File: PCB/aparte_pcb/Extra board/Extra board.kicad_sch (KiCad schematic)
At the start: 4 parts, among them J1 Conn_01x10_Pin, J2 Conn_01x04_Pin, J3 Conn_01x10_Socket, U1 MCP23008-xP

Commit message: extra PCB changes
Multi-line description of commit,
feel free to be detailed.

Signed-off-by: Abel Tim <git@abeltim.com>
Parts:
- removed J3: Conn_01x10_Socket, symbol Connector:Conn_01x10_Socket
- added J3: Conn_01x10_Pin, symbol Connector:Conn_01x10_Pin
- added J4: Conn_01x04_Pin, symbol Connector:Conn_01x04_Pin
- added U2: MCP23017_SP, Package_DIP:DIP-28_W7.62mm, symbol Interface_Expansion:MCP23017_SP
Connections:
- net 5v: now also J2.3 (Pin_3), U1.9 (VSS), J4.3 (Pin_3), U2.10 (VSS); no longer J2.1 (Pin_1), U1.18 (VDD)
- net GND: now also U1.18 (VDD), U1.3 (A2), U1.4 (A1), U1.5 (A0), J4.2 (Pin_2), U2.15 (A0), U2.16 (A1), U2.17 (A2), U2.9 (VDD); no longer U1.9 (VSS)
- net Groen: now also J3.1 (Pin_1); no longer J1.1 (Pin_1), U1.2 (SDA)
- net Rood: now also J3.2 (Pin_2); no longer J1.2 (Pin_2), U1.1 (SCL)
- net blauw: now also J4.1 (Pin_1); no longer J2.3 (Pin_3)
- net pr1: now also J3.10 (Pin_10); no longer J1.10 (Pin_10)
- net pr2: now also J3.9 (Pin_9); no longer J1.9 (Pin_9)
- net pr3: now also J3.8 (Pin_8); no longer J1.8 (Pin_8)
- net pr4: now also J3.7 (Pin_7); no longer J1.7 (Pin_7)
- net pr5: now also J3.6 (Pin_6); no longer J1.6 (Pin_6)
- net pr6: now also J3.5 (Pin_5); no longer J1.5 (Pin_5)
- net pr7: now also J3.4 (Pin_4); no longer J1.4 (Pin_4)
- net pr8: now also J3.3 (Pin_3); no longer J1.3 (Pin_3)
- new net SCL: J1.1 (Pin_1), U1.1 (SCL), U2.12 (SCK)
- new net SDA: J2.1 (Pin_1), U1.2 (SDA), U2.13 (SDA)
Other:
- note added: "LOWER BOARD CONNECTOR"
- note added: "MIDDLE BOARD CONNECTOR"
- moved on the sheet: J2

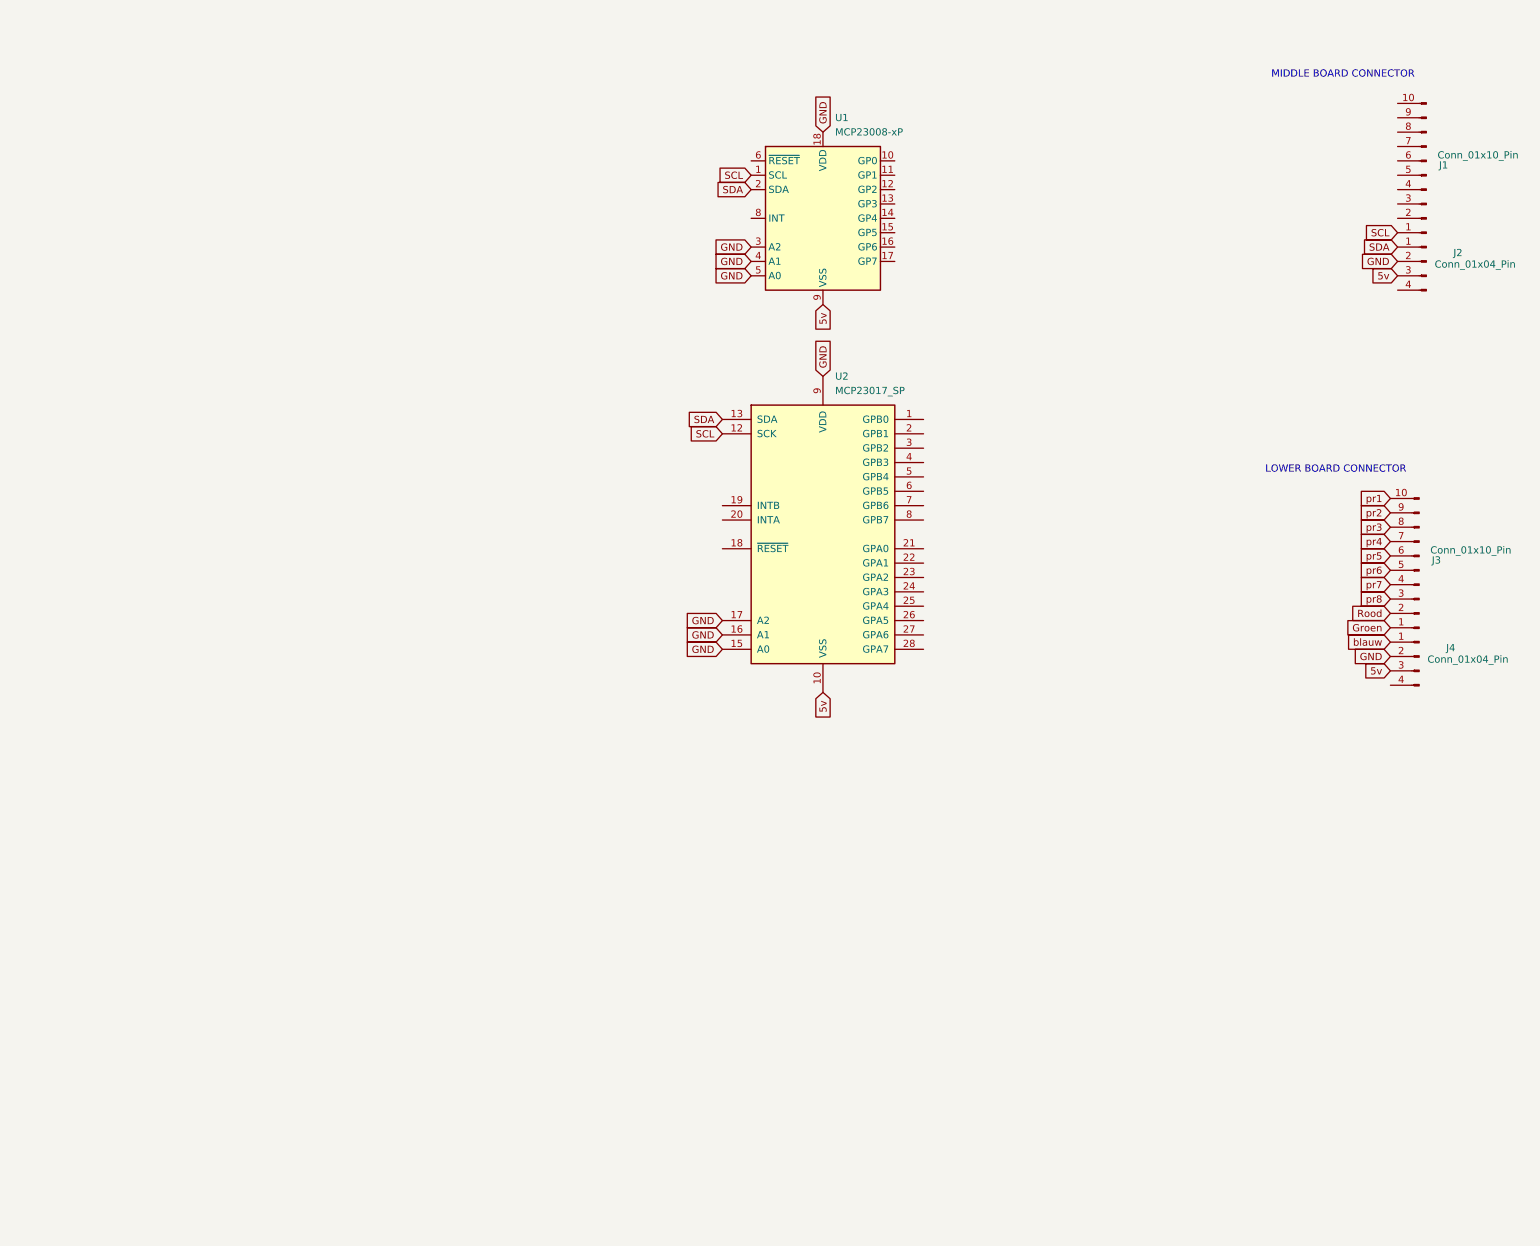
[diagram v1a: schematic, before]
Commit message: almost finished extra pcb
The pcb is designed to be single layerd for simplisity, but there are still two unconnected lines, GND and 5V are now both in two seperate sections. Can connect via an wire or update the PCB. Will not spend a lot of time on it now for it is not shure we will use an PCB or just a board with lots of wires on it.

Signed-off-by: Abel Tim <git@abeltim.com>
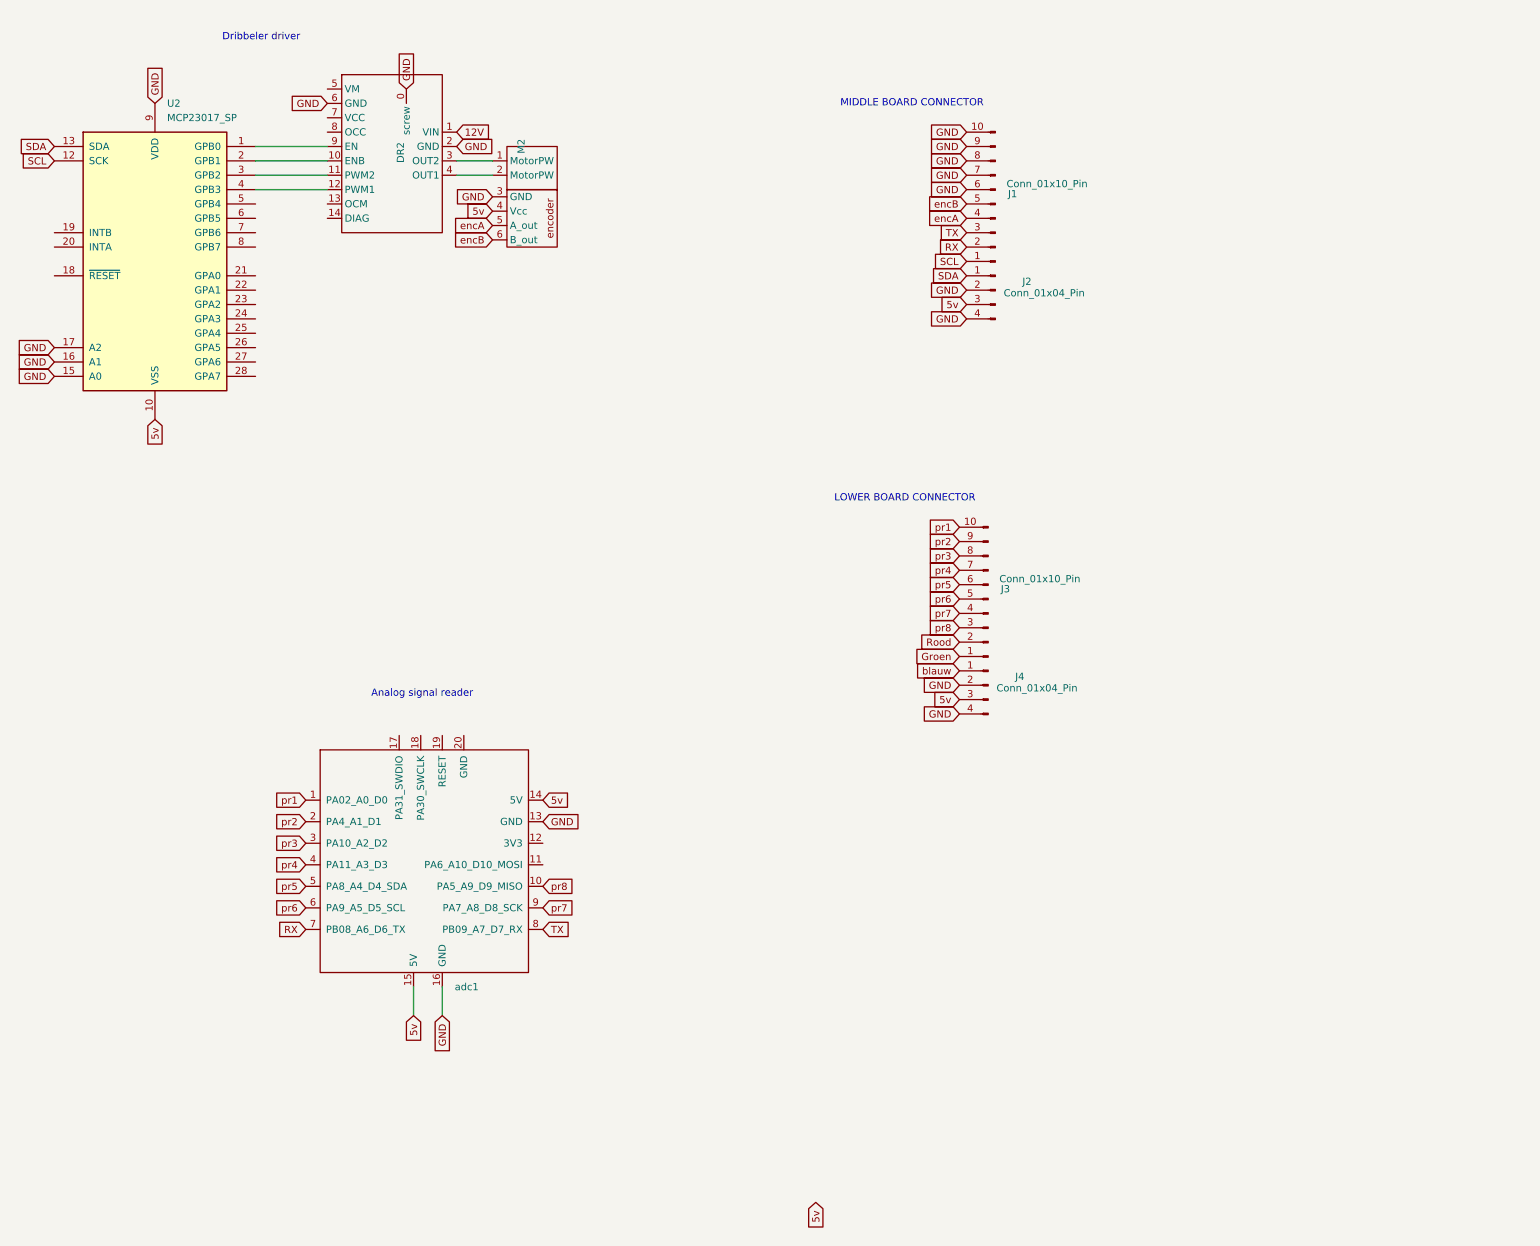
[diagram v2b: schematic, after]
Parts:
- removed U1: MCP23008-xP, Package_DIP:DIP-18_W7.62mm, symbol Interface_Expansion:MCP23008-xP
- added DR2: ~, Library:motordriver, symbol Library:TB9051FTG_2
- added M2: ~, Connector_PinHeader_2.54mm:PinHeader_1x06_P2.54mm_Vertical, symbol Library:pololu_4.4{colon}1_Metal_Gearmotor_25Dx63L_mm_MP_12V_with_48_CPR_Encoder
- added adc1: Seeed Studio XIAO SAMD21, Seeed Studio XIAO Series Library:XIAO-SAMD21-SMD, symbol Library:Seeed Studio XIAO SAMD21
- J1, J3: footprint (none) -> Connector_JST:JST_EH_S10B-EH_1x10_P2.50mm_Horizontal
- J2, J4: footprint (none) -> Connector_JST:JST_EH_S4B-EH_1x04_P2.50mm_Horizontal
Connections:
- net 5v: now also M2.4 (Vcc), adc1.14 (5V), adc1.15 (5V)
- net GND: now also J1.10 (Pin_10), J1.6 (Pin_6), J1.7 (Pin_7), J1.8 (Pin_8), J1.9 (Pin_9), J2.4 (Pin_4), J4.4 (Pin_4), DR2.0 (screw), DR2.2 (GND), DR2.6 (GND), M2.3 (GND), adc1.13 (GND), adc1.16 (GND)
- net pr1: now also adc1.1 (PA02_A0_D0)
- net pr2: now also adc1.2 (PA4_A1_D1)
- net pr3: now also adc1.3 (PA10_A2_D2)
- net pr4: now also adc1.4 (PA11_A3_D3)
- net pr5: now also adc1.5 (PA8_A4_D4_SDA)
- net pr6: now also adc1.6 (PA9_A5_D5_SCL)
- net pr7: now also adc1.9 (PA7_A8_D8_SCK)
- net pr8: now also adc1.10 (PA5_A9_D9_MISO)
- net at U2.1 (GPB0): now also DR2.9 (EN)
- net at U2.2 (GPB1): now also DR2.10 (ENB)
- net at U2.3 (GPB2): now also DR2.11 (PWM2)
- net at U2.4 (GPB3): now also DR2.12 (PWM1)
- net RX: now reaches J1.2 (Pin_2)
- net RX: now also adc1.7 (PB08_A6_D6_TX)
- net TX: now reaches J1.3 (Pin_3)
- net TX: now also adc1.8 (PB09_A7_D7_RX)
- net encA: now reaches J1.4 (Pin_4)
- net encA: now also M2.5 (A_out)
- net encB: now reaches J1.5 (Pin_5)
- net encB: now also M2.6 (B_out)
- new net: DR2.3 (OUT2), M2.1 (MotorPW)
- new net: DR2.4 (OUT1), M2.2 (MotorPW)
- new net 12V: DR2.1 (VIN)
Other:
- note added: "Analog signal reader"
- note added: "Dribbeler driver"
- moved on the sheet: J1, J2, J3, J4, U2

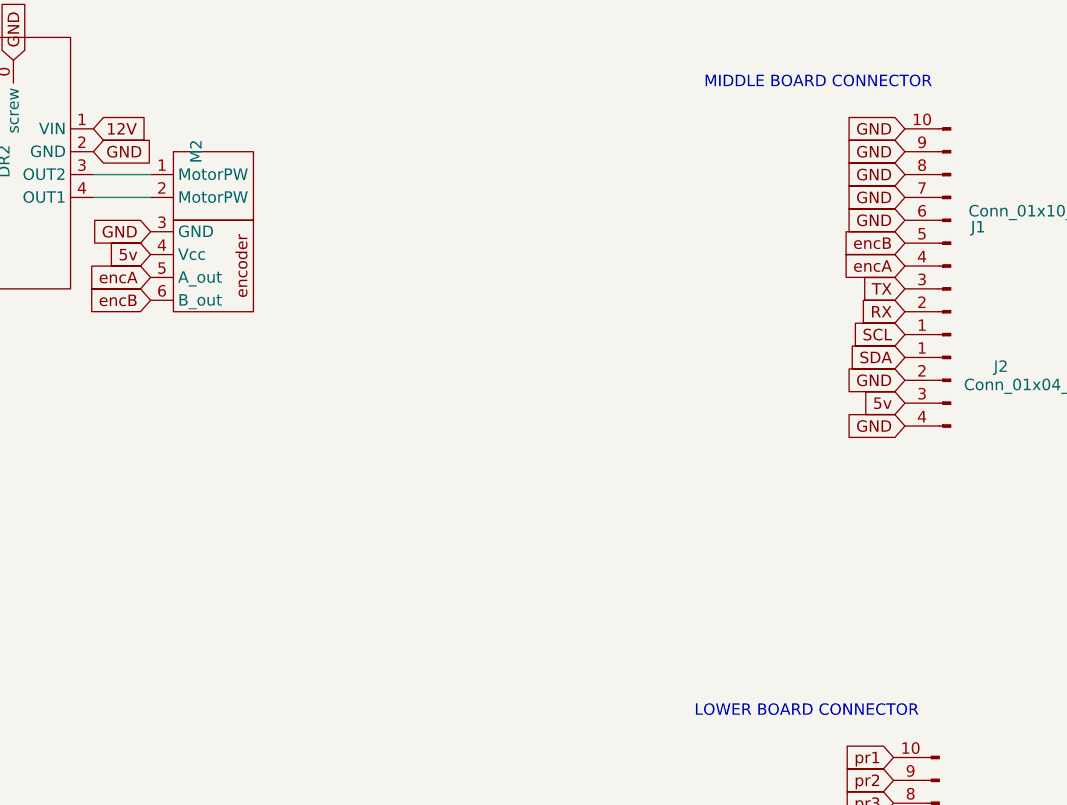
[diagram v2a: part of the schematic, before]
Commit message: Communication module.
Added Communication module to extra PCB, but the power requerments are either our battery power or 3v, but current lines only allow 5v, so either new lines or an power conversion component.
Need to discuss best option with team.
Also TX/RX lines optional but not available. I2C to UART module?
Also need to discuss.

Signed-off-by: Abel Tim <git@abeltim.com>
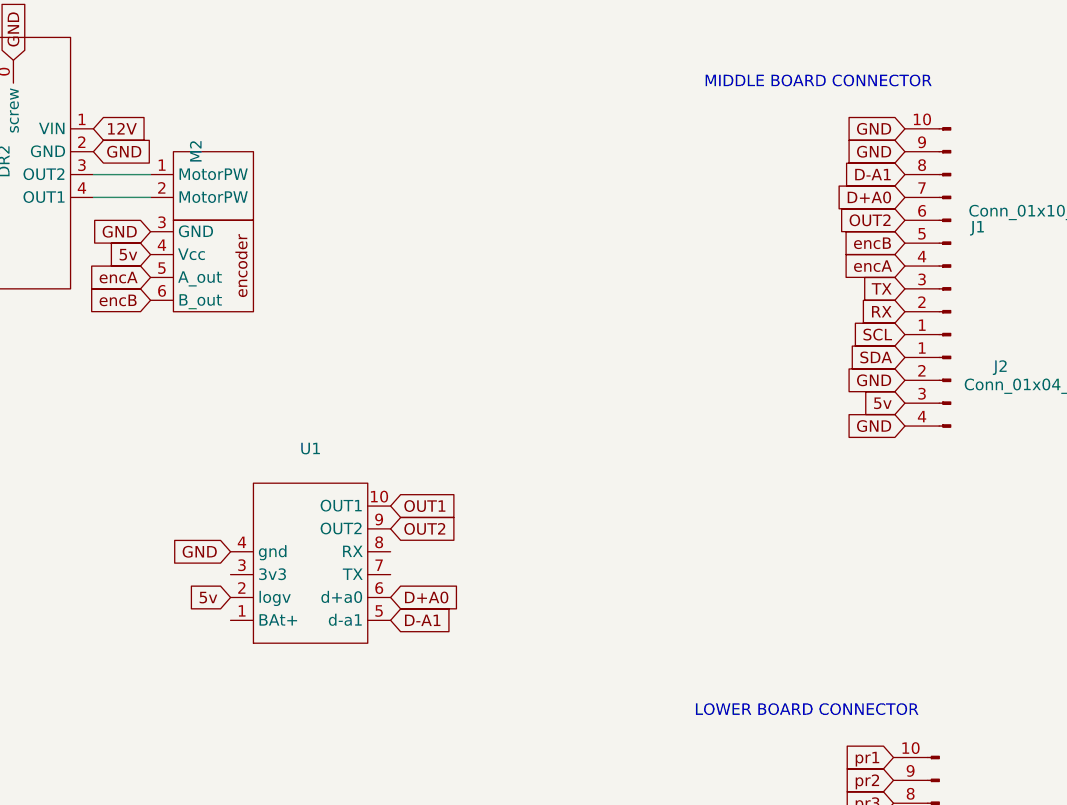
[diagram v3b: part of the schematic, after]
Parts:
- added U1: ~, Library:soccer-communication-module, symbol New_Library:soccer-com-mod
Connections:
- net 5v: now also U1.2 (logv)
- net GND: now also U1.4 (gnd); no longer J1.6 (Pin_6), J1.7 (Pin_7), J1.8 (Pin_8)
- new net D+A0: J1.7 (Pin_7), U1.6 (d+a0)
- new net D-A1: J1.8 (Pin_8), U1.5 (d-a1)
- new net OUT1: U1.10 (OUT1)
- new net OUT2: J1.6 (Pin_6), U1.9 (OUT2)
